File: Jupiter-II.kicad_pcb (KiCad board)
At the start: 2 copper layers, 164.5 x 89.5 mm, 118 parts, among them J1 EXPANSION, J2 KEYBOARD, J3 TAPE, J4 A/V, J5 9Vdc, J6 Conn_02x15_Odd_Even, Q1 BC817, SW1 SW_Push, U1 6116, U10 74LS367, U11 74LS367, U12 74LS367, U13 74LS367, U14 GAL22V10, U15 74HC4040, U16 74HC4040, U17 GAL22V10, U2 27C64, U3 Z80CPU, U4 74LS367, U5 GAL22V10, U6 L7805, U7 74LS166, U8 6116, U9 6116, Y1 6.55 MHz

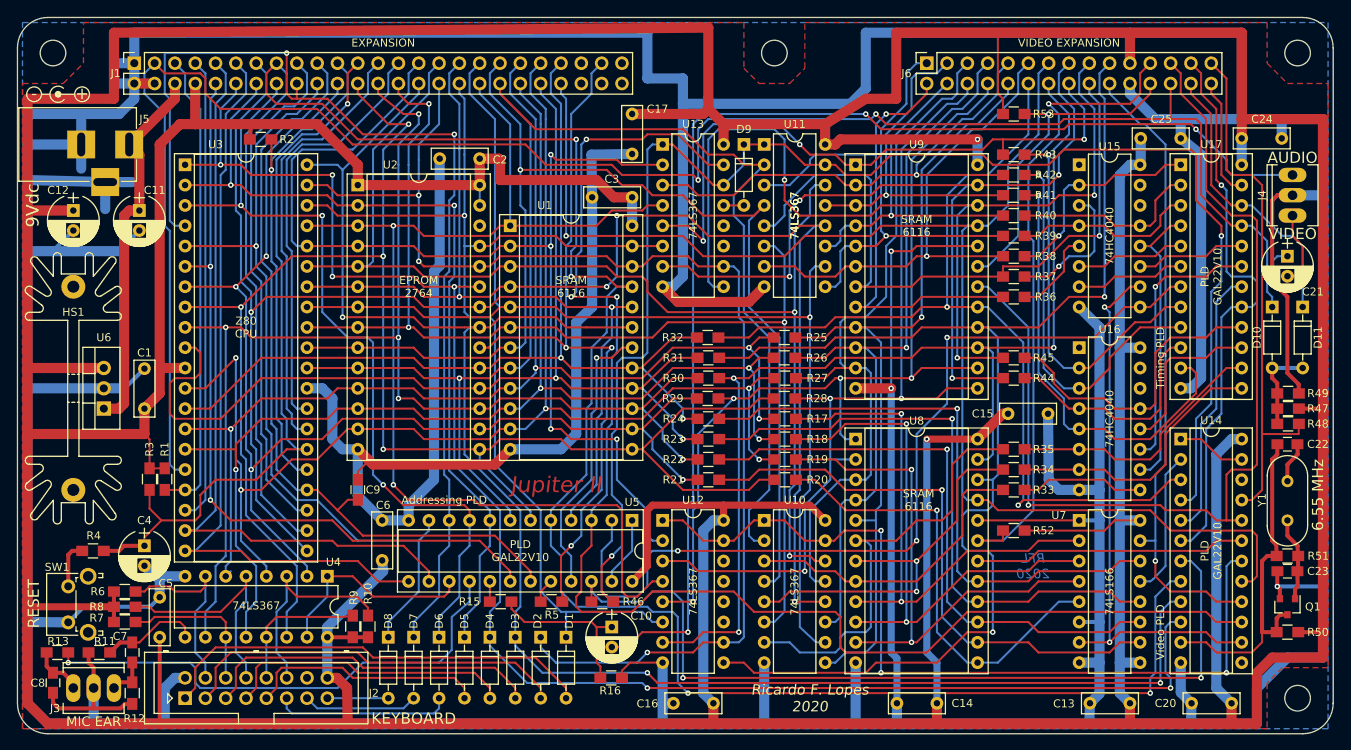
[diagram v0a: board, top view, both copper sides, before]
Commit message: Making it work
Corrected U4 (74LS367) swapped i/o lines
Improved video output circuit
Optimized audio circuit component values
Modified Mic output circuit
Corrected Silk screen swapped labels "R1" and "R3"
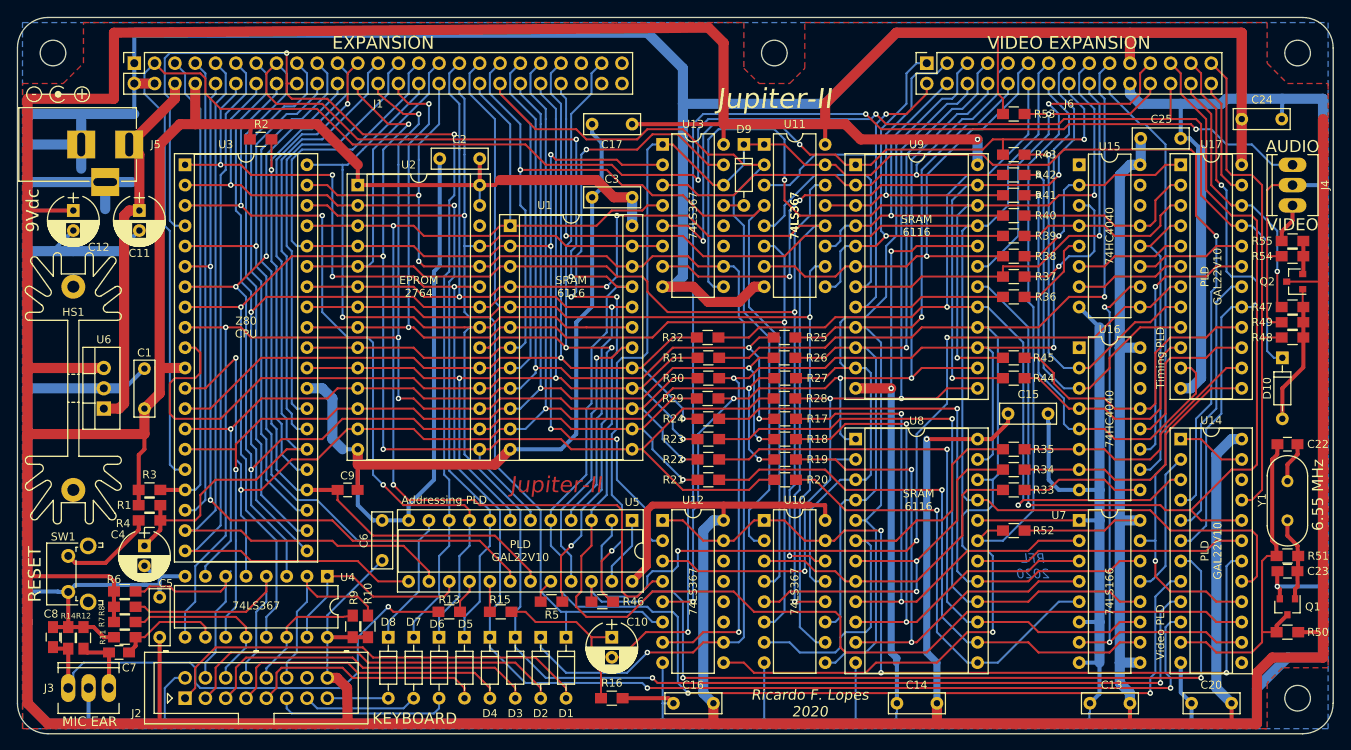
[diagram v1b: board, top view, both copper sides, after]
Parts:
- removed C21: 10u, Capacitors_THT:CP_Radial_D6.3mm_P2.50mm
- removed D11: 1N914, Diodes_THT:D_DO-35_SOD27_P7.62mm_Horizontal
- added Q2: BC817, TO_SOT_Packages_SMD:SOT-23, F.Cu at (244.1, 78.1)
- added R14: 1k, Resistors_SMD:R_0805_HandSoldering, F.Cu at (90.8, 122.6)
- added R54: 470, Resistors_SMD:R_0805_HandSoldering, F.Cu at (243.8, 74.9)
- added R55: 47, Resistors_SMD:R_0805_HandSoldering, F.Cu at (243.8, 73.0)
- C10: value 47u -> 10u
- R13: value 12k -> 5k1
- R15: value 33k -> 5k1
- R47: value 1k -> 2k2
- R48: value 1k -> 1k5
- R49: value 220 -> 2k7
- moved R13 49.2 mm to (138.4, 119.4)
- moved R47 12.7 mm to (243.8, 81.3)
- moved R48 10.8 mm to (243.8, 85.1), turned to 180 degrees
- moved R12 9.21 mm to (92.7, 122.6), turned to 90 degrees
- moved R49 8.91 mm to (243.8, 83.2), turned to 180 degrees
- moved R4 8.03 mm to (101.0, 108.0)
- moved D10 6.84 mm to (242.6, 87.6)
- moved C8 5.72 mm to (88.9, 122.5), turned to 90 degrees
- moved SW1 3.80 mm to (90.8, 116.9)
- moved R11 3.70 mm to (97.9, 122.6)
- moved R1 3.25 mm to (101.0, 106.0), turned to 0 degrees
- moved R16 2.54 mm to (158.8, 130.2)
- moved C24 2.41 mm to (237.5, 57.8)
- moved R3 2.33 mm to (101.0, 104.1), turned to 0 degrees
- moved C7 1.65 mm to (97.2, 124.5), turned to 0 degrees
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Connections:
- D10 pad 1: ~HSYNC -> ~VSYNC
- D10 pad 2: Net-(C21-Pad1) -> Net-(D10-Pad2)
- R47 pad 1: +5V -> Net-(D10-Pad2)
- R47 pad 2: Net-(C21-Pad1) -> ~HSYNC
- R48 pad 1: Net-(C21-Pad1) -> Net-(D10-Pad2)
- R49 pad 1: Net-(C21-Pad1) -> Net-(D10-Pad2)
- U4 pad 10: D5 -> /EAR
- U4 pad 11: /KD1 -> D1
- U4 pad 12: D1 -> /KD1
- U4 pad 13: /KD3 -> D3
- U4 pad 14: D3 -> /KD3
- U4 pad 2: D4 -> /KD4
- U4 pad 3: /KD4 -> D4
- U4 pad 4: D2 -> /KD2
- U4 pad 5: /KD2 -> D2
- U4 pad 6: D0 -> /KD0
- U4 pad 7: /KD0 -> D0
- U4 pad 9: /EAR -> D5
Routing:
- net /MIC: track 62.6 -> 4.30 mm, vias 1 -> 0
- net Net-(C8-Pad1): track 6.57 -> 64.4 mm, vias 0 -> 1
- net Net-(C21-Pad1): track 27.4 -> 0.00 mm
- net GNDD: track 1120.3 -> 1102.5 mm
- net Net-(D10-Pad2): track 0.00 -> 17.3 mm
- net /~RESET: track 93.1 -> 85.3 mm
- net ~VSYNC: track 232.8 -> 240.3 mm
- net Net-(R4-Pad2): track 5.89 -> 12.1 mm
- net +5V: track 1040.1 -> 1035.0 mm
- net Net-(J4-Pad1): track 9.66 -> 5.00 mm
- net Net-(Q2-Pad2): track 0.00 -> 4.16 mm
- net /KD0: track 24.5 -> 28.0 mm
- net /Video/LUMA: track 66.4 -> 63.0 mm
- net /KD1: track 18.8 -> 22.0 mm
- net /KD2: track 30.4 -> 33.3 mm
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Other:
- board text added: "Jupiter-II"
- board text removed: "Jupiter II"

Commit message: Inverted video option
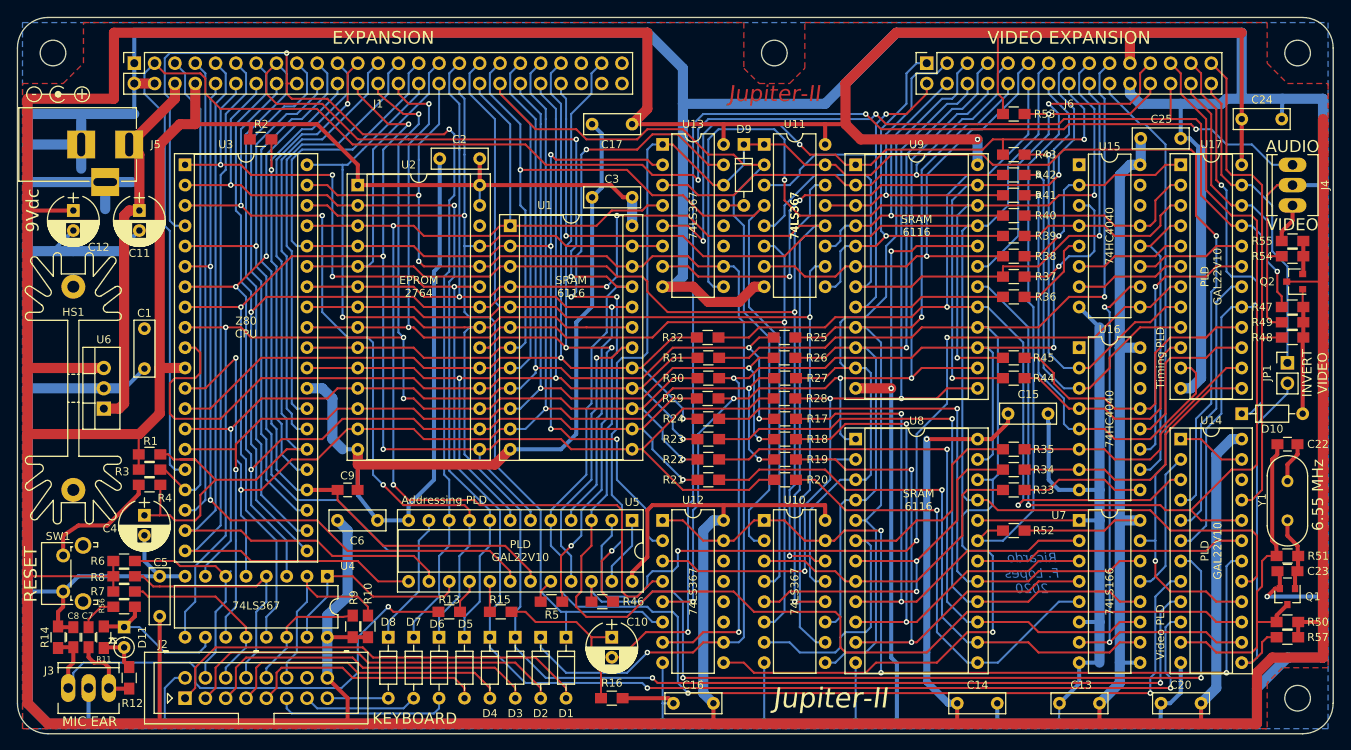
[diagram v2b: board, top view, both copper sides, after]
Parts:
- added D11: 5V1, Diodes_THT:D_DO-35_SOD27_P2.54mm_Vertical_KathodeUp, F.Cu at (97.8, 121.3)
- added JP1: Jumper, Pin_Headers:Pin_Header_Straight_1x02_Pitch2.54mm, F.Cu at (243.2, 88.3)
- added R56: 330, Resistors_SMD:R_0805_HandSoldering, F.Cu at (97.8, 118.7)
- added R57: 10k, Resistors_SMD:R_0805_HandSoldering, F.Cu at (243.2, 122.6)
- moved C1 10.0 mm to (100.3, 84.0), turned to 270 degrees
- moved D10 8.64 mm to (237.5, 94.6), turned to 0 degrees
- moved R12 7.59 mm to (98.4, 127.6)
- moved C6 7.50 mm to (124.5, 108.0), turned to 0 degrees
- moved R1 6.35 mm to (101.0, 99.7)
- moved R4 4.45 mm to (101.0, 103.5)
- moved C7 4.26 mm to (93.3, 122.6), turned to 90 degrees
- moved R6 3.81 mm to (97.8, 113.0)
- moved R7 3.81 mm to (97.8, 116.8)
- moved R8 3.81 mm to (97.8, 114.9)
- moved C13 3.81 mm to (219.7, 130.8)
- moved C20 3.81 mm to (232.4, 130.8)
- moved C4 3.81 mm to (100.3, 107.3)
- moved C5 2.62 mm to (102.2, 119.9)
- moved R11 2.62 mm to (95.2, 122.6), turned to 270 degrees
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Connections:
- C7 pad 2: /EAR -> Net-(C7-Pad2)
- U14 pad 13: (no net) -> /Video/~WBKGND
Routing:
- net /Video/~WBKGND: track 0.00 -> 44.5 mm
- net BLANK: track 15.0 -> 40.4 mm
- net /~RESET: track 85.3 -> 95.6 mm
- net ~VSYNC: track 240.3 -> 247.3 mm
- net +5V: track 1035.0 -> 1028.3 mm
- net GNDD: track 1102.5 -> 1108.3 mm
- net /EAR: track 13.3 -> 18.6 mm
- net Net-(C7-Pad2): track 0.00 -> 4.74 mm
- net Net-(R4-Pad2): track 12.1 -> 15.1 mm
- net /KD2: track 33.3 -> 31.2 mm
- net Net-(D10-Pad2): track 17.3 -> 15.6 mm
- net Net-(C7-Pad1): track 7.85 -> 9.45 mm
- net Net-(C23-Pad1): track 10.5 -> 9.22 mm
- net /KD0: track 28.0 -> 26.8 mm
- net /KD1: track 22.0 -> 23.1 mm
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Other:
- board text added: "INVERT VIDEO"
- board text removed: "RFL 2020"

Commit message: Removing video glitches
Glitches occurs on VIDEN and WAIT lines due to the use of asynchronous counters 74HC4040 (the same occurs when using the 74LS393). Those gliteches are usually controlled by a filtering capacitor in the WAIT line. Here a capacitor was also included at the VIDEN line before WAIT signal generation.
Those glitches can be seen as image interference on screen while the CPU are accessing video memory.
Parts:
- added C18: 1n8, Capacitors_SMD:C_0805_HandSoldering, F.Cu at (210.8, 106.0)
- moved R33 3.13 mm to (210.8, 101.6)
- moved R34 2.64 mm to (210.8, 99.7)
- moved R45 2.64 mm to (210.8, 89.5)
- moved R35 2.22 mm to (210.8, 97.8)
- moved R44 2.22 mm to (210.8, 91.4)
- moved R52 1.93 mm to (210.8, 109.9)
- moved R53 1.93 mm to (210.8, 57.8)
- moved C17 1.46 mm to (160.6, 59.7)
- moved R46 1.42 mm to (158.2, 119.4)
- moved R5 1.27 mm to (151.2, 119.4)
- moved R16 0.90 mm to (158.1, 129.5)
- moved C10 0.63 mm to (158.8, 123.2)
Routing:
- net VIDEN: track 70.8 -> 91.2 mm
- net /Video/~SCRRAM: track 124.9 -> 108.3 mm
- net +5V: track 1028.3 -> 1040.6 mm
- net GNDD: track 1108.3 -> 1114.3 mm
- net /Video/VA7: track 80.5 -> 76.8 mm
- net V7: track 38.4 -> 35.4 mm
- net /Video/INVCHR: track 117.4 -> 114.5 mm
- net Net-(R33-Pad1): track 38.6 -> 41.5 mm
- net Net-(R34-Pad1): track 49.5 -> 52.1 mm
- net /Video/VA9: track 123.1 -> 125.7 mm
- net /Video/~SCRADR: track 187.0 -> 189.5 mm
- net Net-(R35-Pad1): track 54.7 -> 57.1 mm
- net V6: track 29.0 -> 26.7 mm
- net ~WR: track 279.9 -> 277.7 mm
- net A7: track 144.5 -> 142.2 mm
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
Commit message: Video improvement (#6)
* Preparing for expansion

* PLD update for expansion

* PLD update
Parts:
- removed H4: MountingHole, Mounting_Holes:MountingHole_3.2mm_M3
- removed REF**: Symbol_Barrel_Polarity, Symbols:Symbol_Barrel_Polarity
- added JP2: Jumper, Connector_PinHeader_2.54mm:PinHeader_1x02_P2.54mm_Vertical, F.Cu at (141.6, 62.2)
- added R58: 10k, Resistor_SMD:R_0805_2012Metric_Pad1.15x1.40mm_HandSolder, F.Cu at (147.3, 62.2)
- added REF01: Symbol_Barrel_Polarity, Symbol:Symbol_Barrel_Polarity, F.Cu at (94.0, 51.4)
- C12: value 22u -> 10u
- C18, C22, C23, C7, C8, C9: footprint Capacitors_SMD:C_0805_HandSoldering -> Capacitor_SMD:C_0805_2012Metric_Pad1.15x1.40mm_HandSolder
- J3: value TAPE -> Conn_01x03; footprint Sockets_MOLEX_KK-System:Socket_MOLEX-KK-RM2-54mm_Lock_3pin_straight -> Pin_Headers:Pin_Header_Angled_1x03_Pitch2.54mm
- J4: value A/V -> Conn_01x03; footprint Sockets_MOLEX_KK-System:Socket_MOLEX-KK-RM2-54mm_Lock_3pin_straight -> Connectors_Molex:Molex_KK-6410-03_03x2.54mm_Straight
- J5: footprint Connectors:BARREL_JACK -> Connector_BarrelJack:BarrelJack_Horizontal
- R1, R10, R11, R12, R13, R14, R15, R16, R17, R18, R19, R2, R20, R21, R22, R23, R24, R25, R26, R27, R28, R29, R3, R30, R31, R32, R33, R34, R35, R36, R37, R38, R39, R4, R40, R41, R42, R43, R44, R45, R46, R47, R48, R49, R5, R51, R52, R53, R54, R55, R56, R57, R6, R7, R8, R9: footprint Resistors_SMD:R_0805_HandSoldering -> Resistor_SMD:R_0805_2012Metric_Pad1.15x1.40mm_HandSolder
- R50: value 4k7 -> 1k5; footprint Resistors_SMD:R_0805_HandSoldering -> Resistor_SMD:R_0805_2012Metric_Pad1.15x1.40mm_HandSolder
- U2: value 27C64 -> 27C128; footprint Housings_DIP:DIP-28_W15.24mm_Socket -> Package_DIP:DIP-28_W15.24mm
- moved H3 80.6 mm to (244.5, 130.2)
- moved H2 65.4 mm to (244.5, 49.5)
- moved C17 13.0 mm to (172.8, 55.2), turned to 0 degrees
- moved C2 10.7 mm to (131.5, 62.2), turned to 0 degrees
- moved R3 9.16 mm to (100.3, 92.5), turned to 270 degrees
- moved C4 5.72 mm to (100.3, 101.6)
- moved J3 5.24 mm to (94.6, 123.8), turned to 270 degrees
- moved R4 4.26 mm to (99.1, 107.3)
- moved C1 4.10 mm to (99.7, 79.9), turned to 90 degrees
- moved R14 4.07 mm to (92.1, 119.4)
- moved R56 4.02 mm to (99.1, 114.9)
- moved R6 4.02 mm to (99.1, 109.2)
- moved R7 4.02 mm to (99.1, 113.0)
- moved R8 4.02 mm to (99.1, 111.1)
- moved C8 3.42 mm to (90.2, 119.4)
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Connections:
- C10 pad 2: Net-(C10-Pad2) -> SPEAKER
- C22 pad 1: /Video/OSC -> VCLK
- J1 pad 45: (no net) -> Net-(J1-Pad45)
- J1 pad 46: (no net) -> Net-(J1-Pad46)
- J1 pad 48: (no net) -> SPEAKER
- J1 pad 49: (no net) -> Net-(J1-Pad49)
- J1 pad 50: (no net) -> Net-(J1-Pad50)
- J2 pad 14: (no net) -> Net-(J2-Pad14)
- J3 pad 1: Net-(C8-Pad1) -> Net-(C7-Pad1)
- J3 pad 3: Net-(C7-Pad1) -> Net-(C8-Pad1)
- J4 pad 1: Net-(J4-Pad1) -> SPEAKER
- J4 pad 3: Net-(C10-Pad2) -> Net-(J4-Pad3)
- J6 pad 27: VIDEN -> /Video/BORDER
- Q1 pad 3: /Video/OSC -> VCLK
- R50 pad 2: /Video/OSC -> VCLK
- R51 pad 1: /Video/OSC -> VCLK
- R55 pad 1: Net-(J4-Pad1) -> Net-(J4-Pad3)
- U12 pad 11: (no net) -> Net-(U12-Pad11)
- U12 pad 12: (no net) -> Net-(U12-Pad12)
- U12 pad 13: (no net) -> Net-(U12-Pad13)
- U12 pad 14: (no net) -> Net-(U12-Pad14)
- U13 pad 11: (no net) -> Net-(U13-Pad11)
- U13 pad 12: (no net) -> Net-(U13-Pad12)
- U14 pad 11: /Video/OSC -> VCLK
- U14 pad 14: VCLK -> /Video/INV
- U14 pad 22: (no net) -> /Video/BORDER
- U15 pad 1: (no net) -> Net-(U15-Pad1)
- U15 pad 14: (no net) -> Net-(U15-Pad14)
- U15 pad 15: (no net) -> Net-(U15-Pad15)
- U16 pad 1: (no net) -> Net-(U16-Pad1)
- U16 pad 14: (no net) -> Net-(U16-Pad14)
- U16 pad 15: (no net) -> Net-(U16-Pad15)
- U2 pad 26: (no net) -> Net-(JP2-Pad2)
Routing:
- net SPEAKER: track 0.00 -> 168.8 mm, vias 0 -> 4
- net Net-(C10-Pad2): track 154.5 -> 0.00 mm, vias 3 -> 0
- net /Video/BORDER: track 0.00 -> 59.0 mm, vias 0 -> 1
- net /Video/OSC: track 43.1 -> 0.00 mm
- net VIDEN: track 91.2 -> 54.5 mm, vias 1 -> 0
- net VCLK: track 68.4 -> 102.4 mm
- net Net-(JP2-Pad2): track 0.00 -> 17.4 mm
- net /~NMI: track 60.3 -> 70.1 mm
- net ~VHOLD: track 179.2 -> 169.4 mm, vias 3 -> 1
- net +5V: track 1040.6 -> 1032.7 mm
- net /~RESET: track 95.6 -> 89.2 mm
- net Net-(J4-Pad1): track 5.00 -> 0.00 mm
- net Net-(R4-Pad2): track 15.1 -> 10.1 mm
- net Net-(J4-Pad3): track 0.00 -> 4.87 mm
- net A6: track 137.8 -> 142.3 mm
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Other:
- board text added: "16K EPROM"
- board text added: "2K SRAM"
- board text added: "2K SRAM Character Memory"
- board text added: "2K SRAM Screen Memory"
- board text added: "A"
- board text added: "A/V out"
- board text added: "Address PLD"
- board text added: "EAR"
- board text added: "GND"
- board text added: "Jupiter ACE ROM"
- board text added: "MIC"
- board text added: "May 2020"
- board text added: "V"
- board text removed: "AUDIO"
- board text removed: "Addressing PLD"
- board text removed: "EPROM 2764"
- board text removed: "MIC EAR"
- board text removed: "PLD GAL22V10"
- board text removed: "SRAM 6116"
- board text removed: "VIDEO"
- board text removed: "Z80 CPU"
